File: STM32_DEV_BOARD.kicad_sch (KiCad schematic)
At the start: 20 parts, among them J1 USB_C_Receptacle_USB2.0_14P, SW1 SW_SPDT, U1 STM32F103C8T6, Y1 16MHz

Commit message: Schematic ready
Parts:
- added C12: 1u, symbol Device:C
- added C13: 4u7, symbol Device:C
- added D1: LED, symbol Device:LED
- added J2, J3, J4: Conn_01x04_Pin, symbol Connector:Conn_01x04_Pin
- added R5, R6, R7: 1k5, symbol Device:R
- added U3: LDL1117S33R, Package_TO_SOT_SMD:SOT-223-3_TabPin2, symbol ctm:LDL1117S33R
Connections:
- net +3.3V: now also C13.1, D1.2 (A), J2.1 (Pin_1), J3.1 (Pin_1), J4.1 (Pin_1), R6.2, R7.2, U3.2 (VOUT)
- net GND: now also C12.2, C13.2, J2.4 (Pin_4), J3.4 (Pin_4), J4.4 (Pin_4), R5.1, U3.1 (GND)
- net SWCLK: now also J2.3 (Pin_3)
- net SWDIO: now also J2.2 (Pin_2)
- net VBUS: now also C12.1, U3.3 (VIN)
- net I2C_SCL: now reaches U1.21 (PB10)
- net I2C_SCL: now also J4.2 (Pin_2), R7.1
- net I2C_SDA: now reaches U1.22 (PB11)
- net I2C_SDA: now also J4.3 (Pin_3), R6.1
- net USART_TX: now reaches U1.42 (PB6)
- net USART_TX: now also J3.2 (Pin_2)
- net USART_RX: now reaches U1.43 (PB7)
- net USART_RX: now also J3.3 (Pin_3)
- new net PWR_LED_Kath: D1.1 (K), R5.2
- no-connect marks 0 -> 27
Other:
- note added: "- VBUS from USB connector (nom +5V) - In/Out caps according to datasheet (LDL1117S33)"
- note added: "STM32 Demo Board"
- note removed: "Analog Supply"
- note removed: "Decoupling Caps"
- moved on the sheet: C1, C10, C11, C2, C3, C4, C5, C6, C7, C8, C9, FB1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

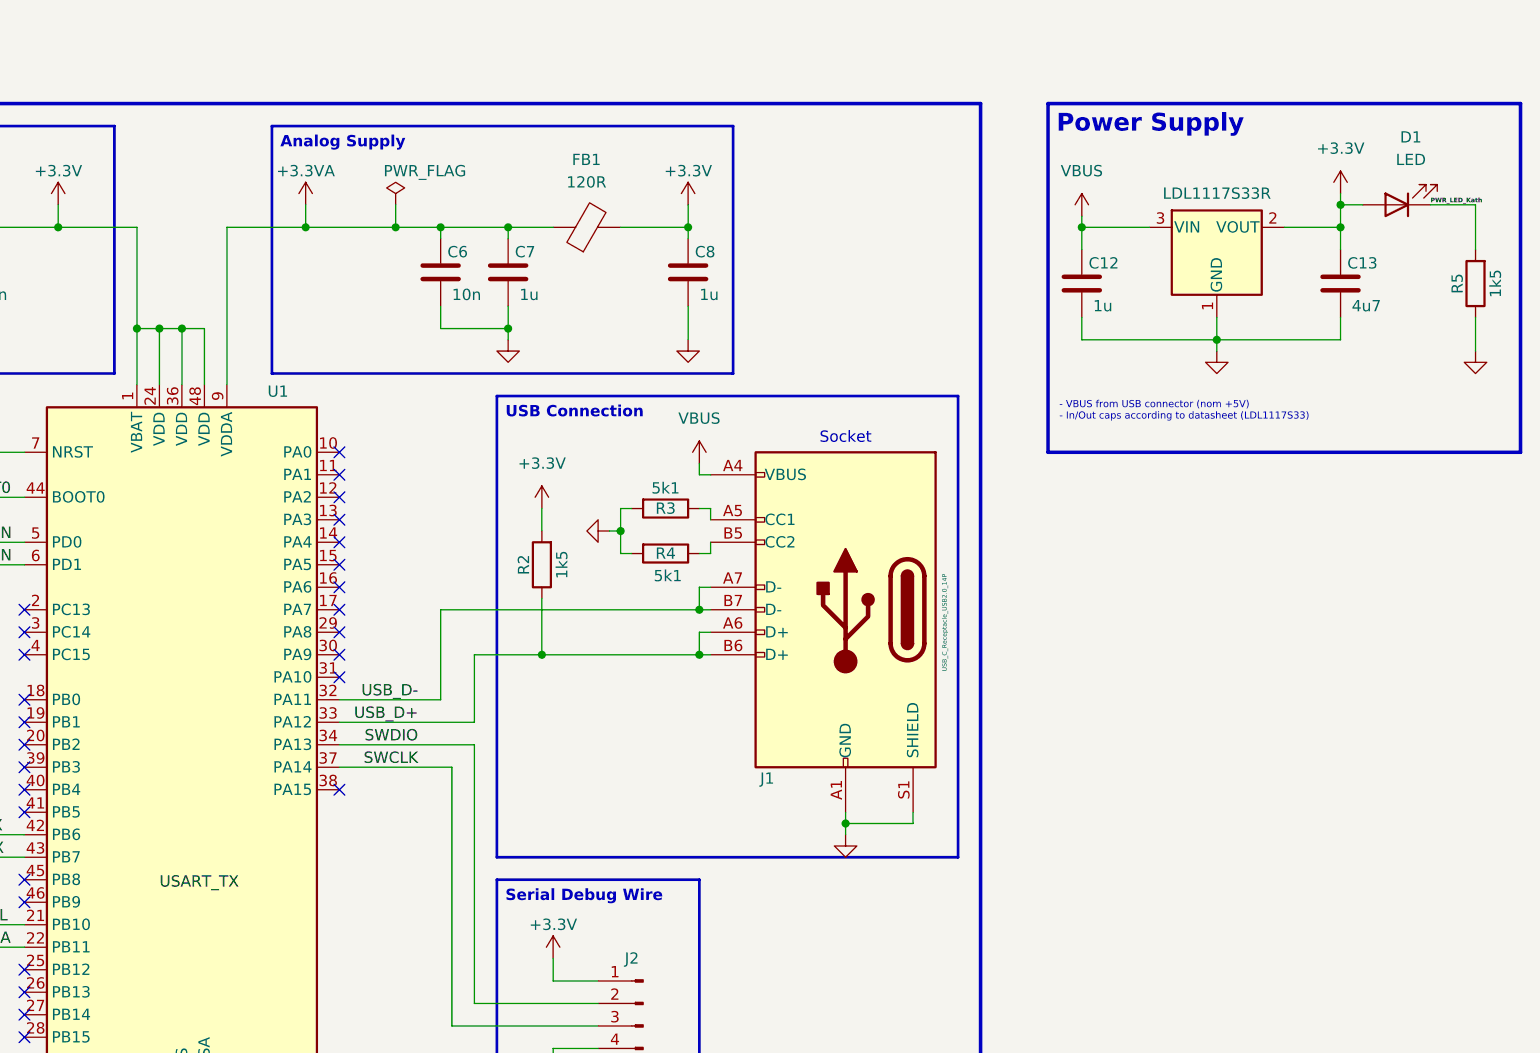
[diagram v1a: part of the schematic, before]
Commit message: Schematic footprints asignment
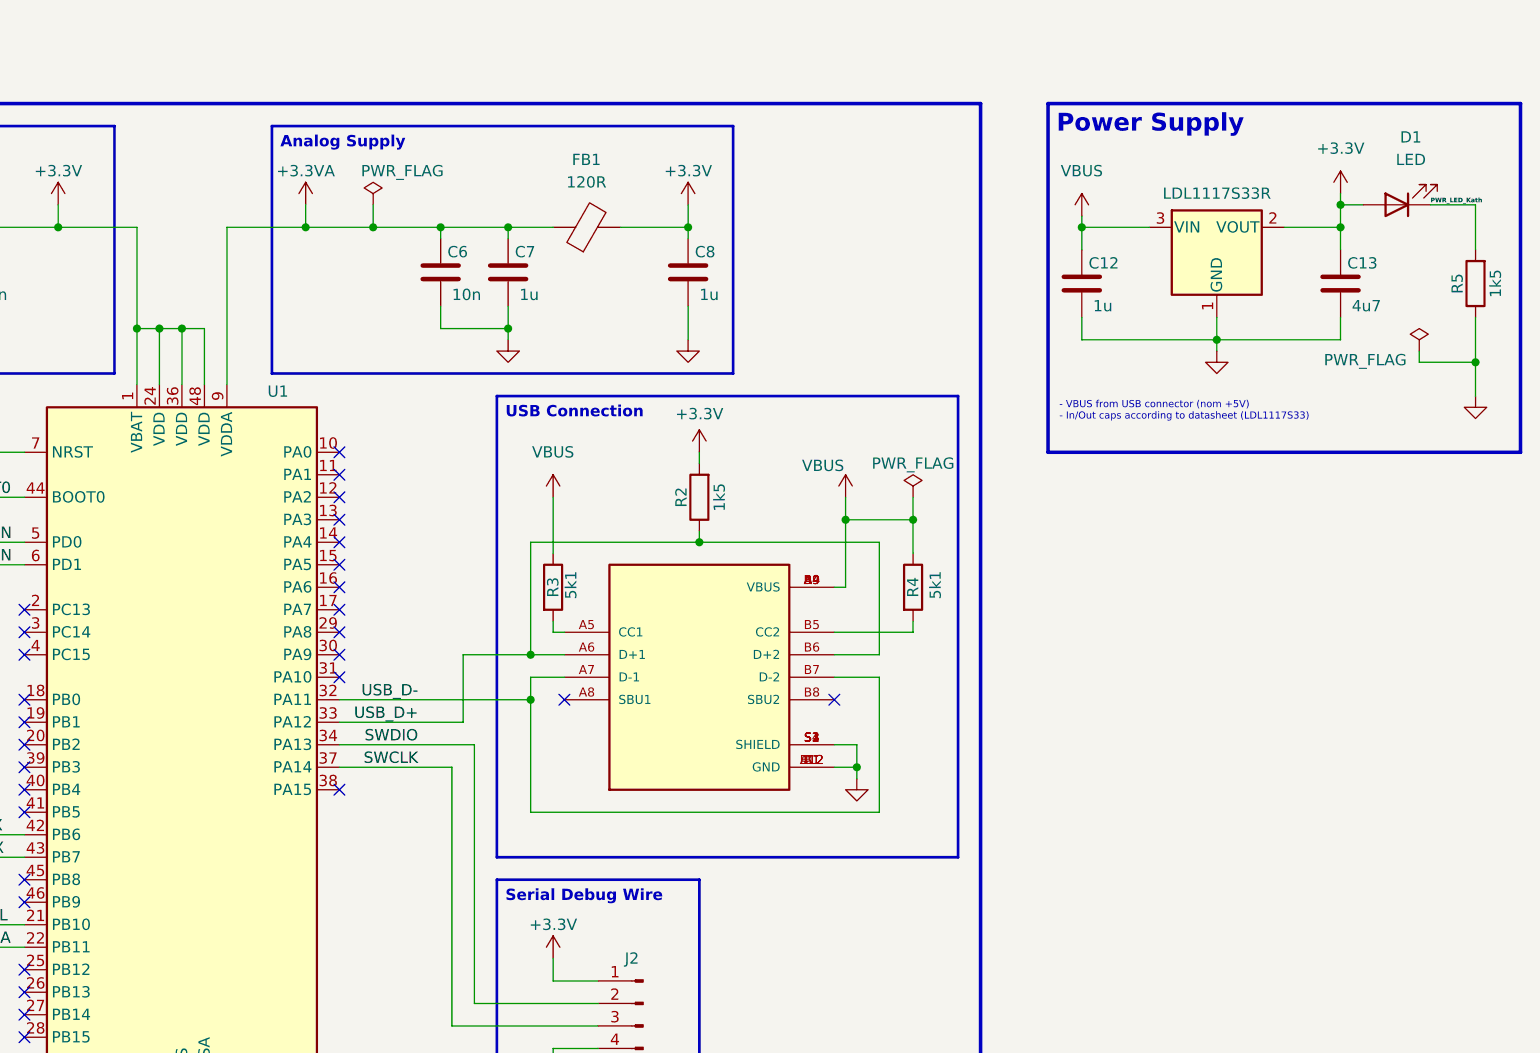
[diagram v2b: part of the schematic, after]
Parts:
- removed J1: USB_C_Receptacle_USB2.0_14P, symbol Connector:USB_C_Receptacle_USB2.0_14P
- added J5: 629722000214, ctm:WURTH_629722000214, symbol ctm:629722000214
- C1, C10, C11, C12, C13, C2, C3, C4, C5, C6, C7, C8, C9: footprint (none) -> Capacitor_SMD:C_0603_1608Metric_Pad1.08x0.95mm_HandSolder
- D1: footprint (none) -> LED_SMD:LED_0805_2012Metric_Pad1.15x1.40mm_HandSolder
- FB1: footprint (none) -> Inductor_SMD:L_0805_2012Metric_Pad1.15x1.40mm_HandSolder
- J2, J3, J4: footprint (none) -> Connector_PinHeader_2.54mm:PinHeader_1x04_P2.54mm_Vertical
- R1, R2, R3, R4, R5, R6, R7: footprint (none) -> Resistor_SMD:R_0805_2012Metric_Pad1.20x1.40mm_HandSolder
- SW1: footprint (none) -> Button_Switch_THT:SW_E-Switch_EG1224_SPDT_Angled
- Y1: footprint (none) -> Crystal:Crystal_SMD_3225-4Pin_3.2x2.5mm
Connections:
- net GND: now also J5.A1 (GND), J5.A12 (GND), J5.B1 (GND), J5.B12 (GND), J5.S1 (SHIELD), J5.S2 (SHIELD), J5.S3 (SHIELD), J5.S4 (SHIELD); no longer R3.2, R4.2
- net USB_D+: now also J5.A6 (D+1), J5.B6 (D+2)
- net USB_D-: now also J5.A7 (D-1), J5.B7 (D-2)
- net VBUS: now also R3.1, R4.1, J5.A4 (VBUS), J5.A9 (VBUS), J5.B4 (VBUS), J5.B9 (VBUS)
- new net: J5.B5 (CC2), R4.2
- new net: J5.A5 (CC1), R3.2
- no-connect marks 27 -> 29
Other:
- note removed: "Socket"
- company: (none) -> Lukas Eppacher
- moved on the sheet: R2, R3, R4

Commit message: complete layout
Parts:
- removed SW1: SW_SPDT, Button_Switch_THT:SW_E-Switch_EG1224_SPDT_Angled, symbol Switch:SW_SPDT
- added H1, H2, H3, H4: MountingHole, MountingHole:MountingHole_2.2mm_M2, symbol Mechanical:MountingHole
- added SW1: SW_Wuerth_450301014042, Button_Switch_THT:SW_Slide-03_Wuerth-WS-SLTV_10x2.5x6.4_P2.54mm, symbol Switch:SW_Wuerth_450301014042
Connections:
- net +3.3V: now also SW1.2 (C)
- net GND: now also SW1.3 (A)
- net HSE_IN: no longer C11.1, U1.6 (PD1), Y1.3
- net SW_BOOT0: now also SW1.1 (B)
- new net HSE_OUT: C11.1, U1.6 (PD1), Y1.3
